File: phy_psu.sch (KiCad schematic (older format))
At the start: 54 parts

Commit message: sch: Make ERC happy with dummy power outputs
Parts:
- added DS? (x4): DummySupply, symbol pimouss-motherboard:DummySupply
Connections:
- net +1V8A: now also DS?.~ (Dummy)
- net +3V3A: now also DS?.~ (Dummy)
- net VphyDVDD: now also DS?.~ (Dummy)
- net VphyVDDC: now also DS?.~ (Dummy)
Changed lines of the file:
@@
 	8600 2900 8600 2950
 Connection ~ 8600 2900
+$Comp
+L pimouss-motherboard:DummySupply DS?
+U 1 1 5E44288B
+P 2400 1600
+F 0 "DS?" H 2400 1600 50  0001 C CNN
+F 1 "DummySupply" H 2400 1600 50  0001 C CNN
+F 2 "" H 2400 1600 50  0001 C CNN
+F 3 "" H 2400 1600 50  0001 C CNN
+	1    2400 1600
+	0    1    1    0
+$EndComp
+$Comp
+L pimouss-motherboard:DummySupply DS?
+U 1 1 5E443971
+P 2400 2800
+F 0 "DS?" H 2400 2800 50  0001 C CNN
+F 1 "DummySupply" H 2400 2800 50  0001 C CNN
+F 2 "" H 2400 2800 50  0001 C CNN
+F 3 "" H 2400 2800 50  0001 C CNN
+	1    2400 2800
+	0    1    1    0
+$EndComp
+$Comp
+L pimouss-motherboard:DummySupply DS?
+U 1 1 5E444394
+P 2400 4000
+F 0 "DS?" H 2400 4000 50  0001 C CNN
+F 1 "DummySupply" H 2400 4000 50  0001 C CNN
+F 2 "" H 2400 4000 50  0001 C CNN
+F 3 "" H 2400 4000 50  0001 C CNN
+	1    2400 4000
+	0    1    1    0
+$EndComp
+$Comp
+L pimouss-motherboard:DummySupply DS?
+U 1 1 5E444BDF
+P 2400 5200
+F 0 "DS?" H 2400 5200 50  0001 C CNN
+F 1 "DummySupply" H 2400 5200 50  0001 C CNN
+F 2 "" H 2400 5200 50  0001 C CNN
+F 3 "" H 2400 5200 50  0001 C CNN
+	1    2400 5200
+	0    1    1    0
+$EndComp
 $EndSCHEMATC

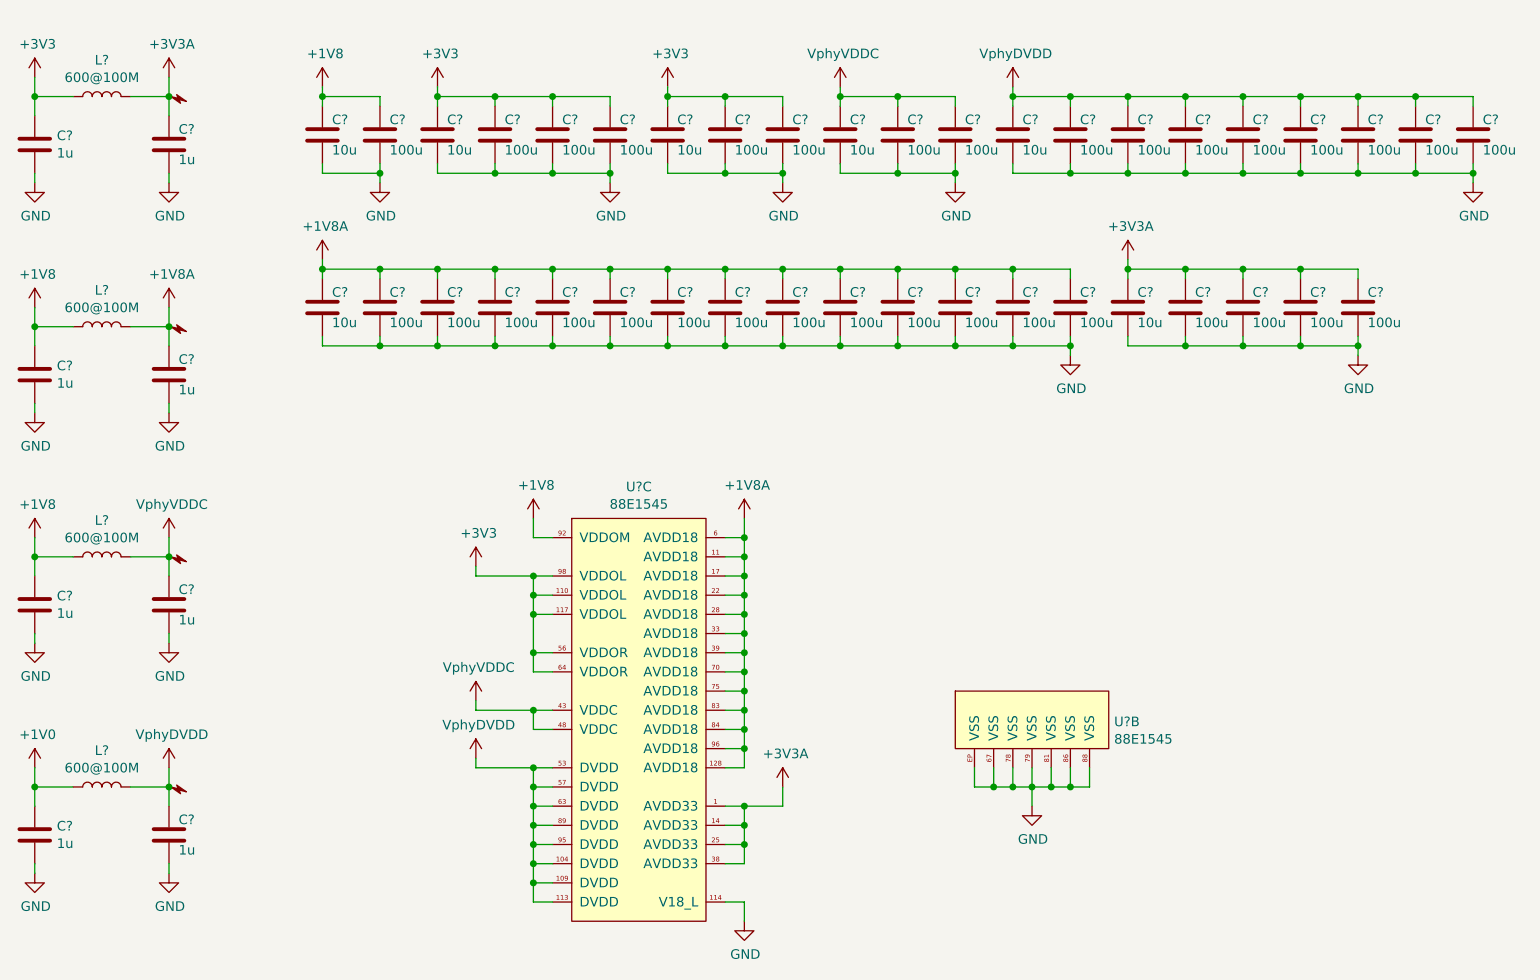
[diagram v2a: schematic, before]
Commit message: sch: Annotate & associate symbols with footprints
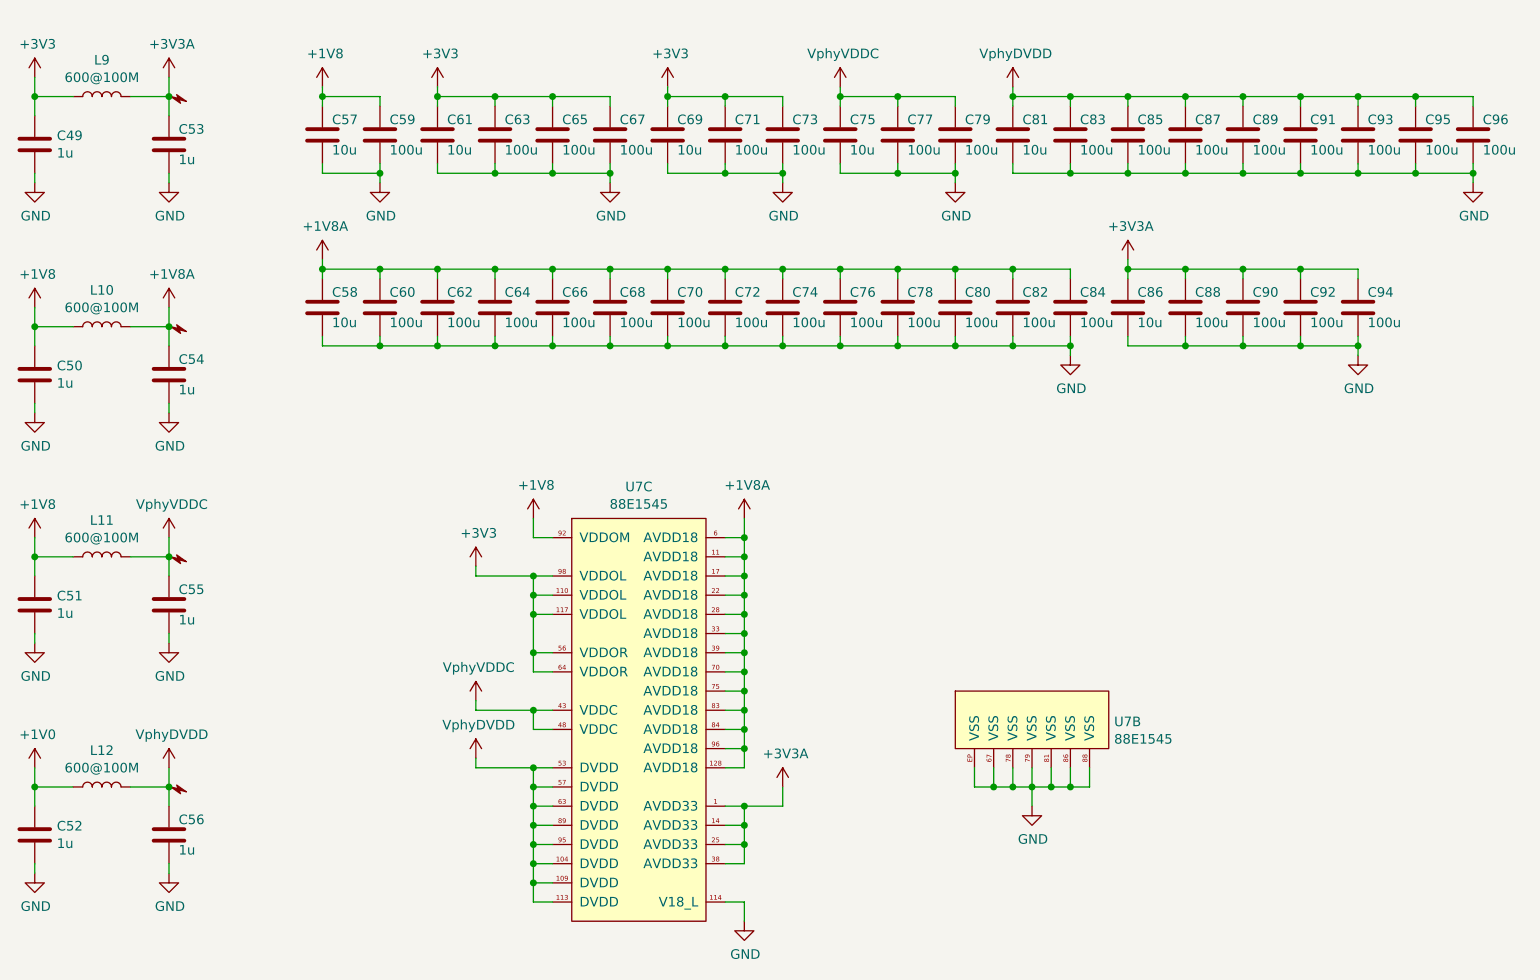
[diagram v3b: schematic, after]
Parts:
- removed DS? (x4): DummySupply, symbol pimouss-motherboard:DummySupply
- C49, C50, C51, C52, C53, C54, C55, C56, C57, C58, C59, C60, C61, C62, C63, C64, C65, C66, C67, C68, C69, C70, C71, C72, C73, C74, C75, C76, C77, C78, C79, C80, C81, C82, C83, C84, C85, C86, C87, C88, C89, C90, C91, C92, C93, C94, C95, C96: renamed from C?; footprint (none) -> Capacitor_SMD:C_0603_1608Metric
- L10, L11, L12, L9: renamed from L?; footprint (none) -> Inductor_SMD:L_0603_1608Metric
- gave numbers to parts that had none: 1

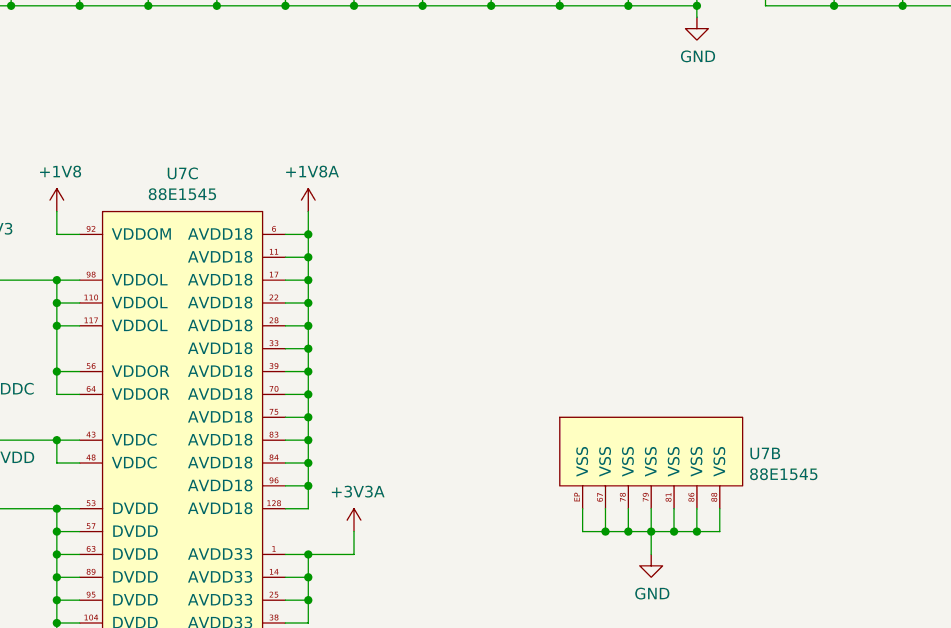
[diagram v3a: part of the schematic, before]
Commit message: lib, sch: Fix connectors refdes letter
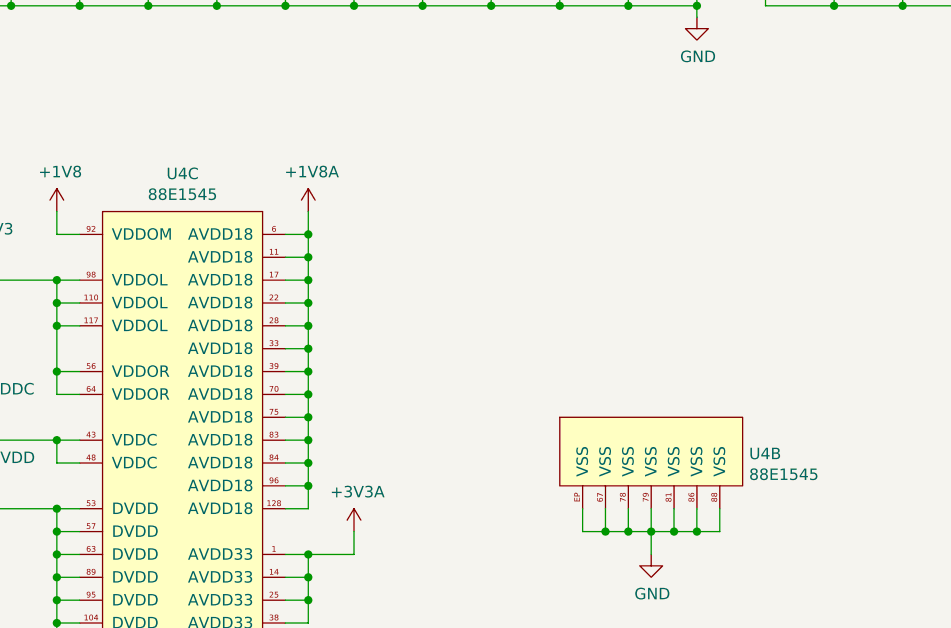
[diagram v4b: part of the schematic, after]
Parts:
- renumbered U7 to U4
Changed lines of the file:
@@
 $EndDescr
 $Comp
-L pimouss-motherboard:88E1545 U7
+L pimouss-motherboard:88E1545 U4
 U 2 1 5C7D4C8A
 P 6500 4700
-F 0 "U7" H 7328 4540 50  0000 L CNN
+F 0 "U4" H 7328 4540 50  0000 L CNN
 F 1 "88E1545" H 7328 4449 50  0000 L CNN
 F 2 "pimouss-motherboard:LQFP-128-1EP_14x20mm_P0.5mm_EP3.93x6.42mm" H 7950 2900 50  0001 C CNN
@@
 $EndComp
 $Comp
-L pimouss-motherboard:88E1545 U7
+L pimouss-motherboard:88E1545 U4
 U 3 1 5C7D4CD7
 P 4500 3800
-F 0 "U7" H 4850 3965 50  0000 C CNN
+F 0 "U4" H 4850 3965 50  0000 C CNN
 F 1 "88E1545" H 4850 3874 50  0000 C CNN
 F 2 "pimouss-motherboard:LQFP-128-1EP_14x20mm_P0.5mm_EP3.93x6.42mm" H 5950 2000 50  0001 C CNN

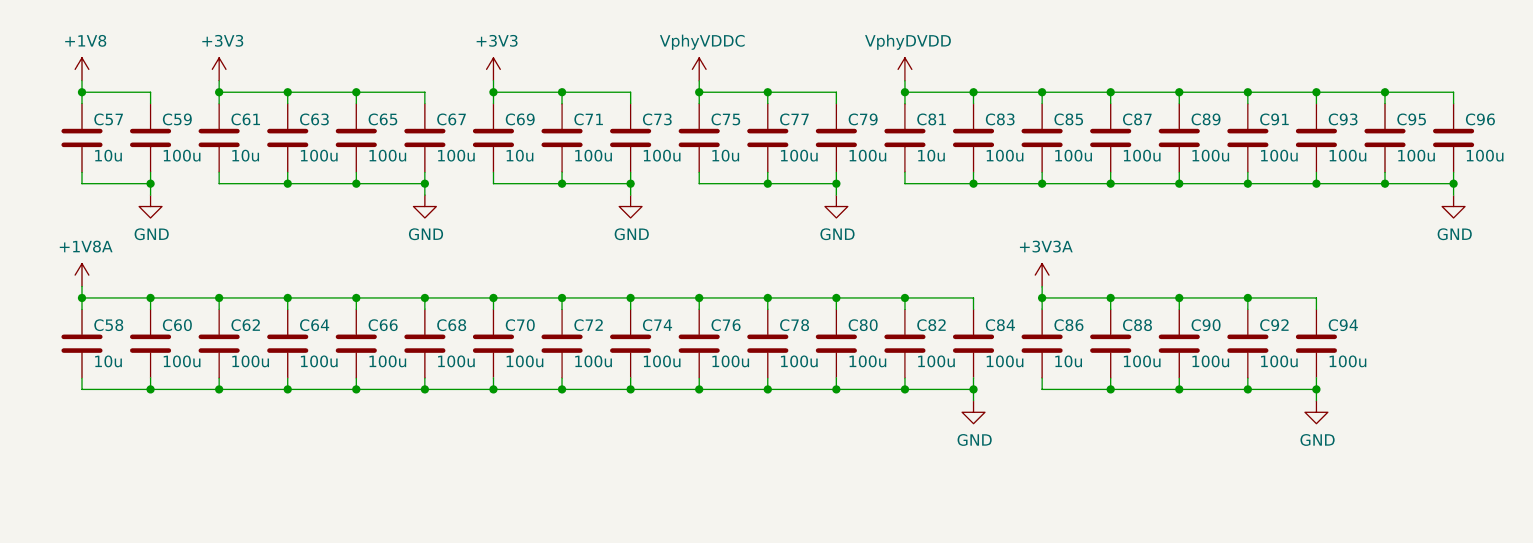
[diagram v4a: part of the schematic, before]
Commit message: sch: Change PHY decoupling caps from 100u to 100n
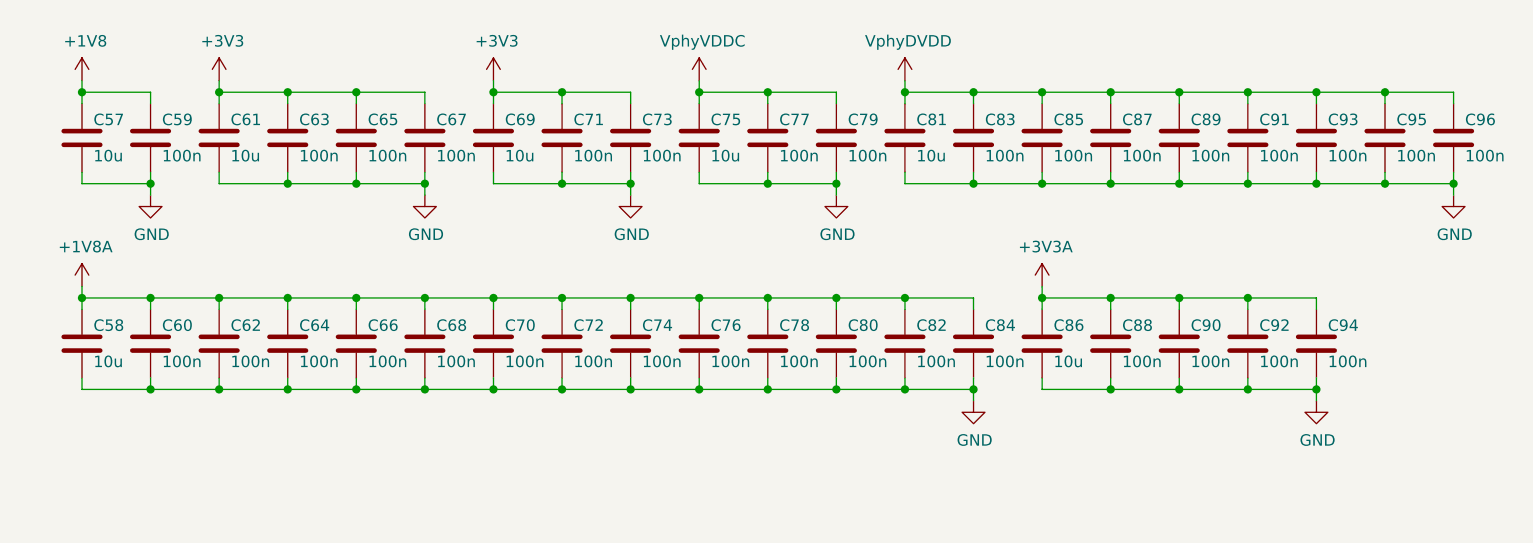
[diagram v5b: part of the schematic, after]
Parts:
- C59, C60, C62, C63, C64, C65, C66, C67, C68, C70, C71, C72, C73, C74, C76, C77, C78, C79, C80, C82, C83, C84, C85, C87, C88, C89, C90, C91, C92, C93, C94, C95, C96: value 100u -> 100n
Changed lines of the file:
@@
 P 3500 1800
 F 0 "C59" H 3550 1850 50  0000 L BNN
-F 1 "100u" H 3550 1750 50  0000 L TNN
+F 1 "100n" H 3550 1750 50  0000 L TNN
 F 2 "Capacitor_SMD:C_0603_1608Metric" H 3538 1650 50  0001 C CNN
 F 3 "~" H 3500 1800 50  0001 C CNN
@@
 P 4100 1800
 F 0 "C63" H 4150 1850 50  0000 L BNN
-F 1 "100u" H 4150 1750 50  0000 L TNN
+F 1 "100n" H 4150 1750 50  0000 L TNN
 F 2 "Capacitor_SMD:C_0603_1608Metric" H 4138 1650 50  0001 C CNN
 F 3 "~" H 4100 1800 50  0001 C CNN
@@
 P 4400 1800
 F 0 "C65" H 4450 1850 50  0000 L BNN
-F 1 "100u" H 4450 1750 50  0000 L TNN
+F 1 "100n" H 4450 1750 50  0000 L TNN
 F 2 "Capacitor_SMD:C_0603_1608Metric" H 4438 1650 50  0001 C CNN
 F 3 "~" H 4400 1800 50  0001 C CNN
@@
 P 4700 1800
 F 0 "C67" H 4750 1850 50  0000 L BNN
-F 1 "100u" H 4750 1750 50  0000 L TNN
+F 1 "100n" H 4750 1750 50  0000 L TNN
 F 2 "Capacitor_SMD:C_0603_1608Metric" H 4738 1650 50  0001 C CNN
 F 3 "~" H 4700 1800 50  0001 C CNN
@@
 P 5300 1800
 F 0 "C71" H 5350 1850 50  0000 L BNN
-F 1 "100u" H 5350 1750 50  0000 L TNN
+F 1 "100n" H 5350 1750 50  0000 L TNN
 F 2 "Capacitor_SMD:C_0603_1608Metric" H 5338 1650 50  0001 C CNN
 F 3 "~" H 5300 1800 50  0001 C CNN
@@
 P 5600 1800
 F 0 "C73" H 5650 1850 50  0000 L BNN
-F 1 "100u" H 5650 1750 50  0000 L TNN
+F 1 "100n" H 5650 1750 50  0000 L TNN
 F 2 "Capacitor_SMD:C_0603_1608Metric" H 5638 1650 50  0001 C CNN
 F 3 "~" H 5600 1800 50  0001 C CNN
@@
 P 6200 1800
 F 0 "C77" H 6250 1850 50  0000 L BNN
-F 1 "100u" H 6250 1750 50  0000 L TNN
+F 1 "100n" H 6250 1750 50  0000 L TNN
 F 2 "Capacitor_SMD:C_0603_1608Metric" H 6238 1650 50  0001 C CNN
 F 3 "~" H 6200 1800 50  0001 C CNN
@@
 P 6500 1800
 F 0 "C79" H 6550 1850 50  0000 L BNN
-F 1 "100u" H 6550 1750 50  0000 L TNN
+F 1 "100n" H 6550 1750 50  0000 L TNN
 F 2 "Capacitor_SMD:C_0603_1608Metric" H 6538 1650 50  0001 C CNN
 F 3 "~" H 6500 1800 50  0001 C CNN
@@
 P 7100 1800
 F 0 "C83" H 7150 1850 50  0000 L BNN
-F 1 "100u" H 7150 1750 50  0000 L TNN
+F 1 "100n" H 7150 1750 50  0000 L TNN
 F 2 "Capacitor_SMD:C_0603_1608Metric" H 7138 1650 50  0001 C CNN
 F 3 "~" H 7100 1800 50  0001 C CNN
@@
 P 7400 1800
 F 0 "C85" H 7450 1850 50  0000 L BNN
-F 1 "100u" H 7450 1750 50  0000 L TNN
+F 1 "100n" H 7450 1750 50  0000 L TNN
 F 2 "Capacitor_SMD:C_0603_1608Metric" H 7438 1650 50  0001 C CNN
 F 3 "~" H 7400 1800 50  0001 C CNN
@@
 P 7700 1800
 F 0 "C87" H 7750 1850 50  0000 L BNN
-F 1 "100u" H 7750 1750 50  0000 L TNN
+F 1 "100n" H 7750 1750 50  0000 L TNN
 F 2 "Capacitor_SMD:C_0603_1608Metric" H 7738 1650 50  0001 C CNN
 F 3 "~" H 7700 1800 50  0001 C CNN
@@
 P 8000 1800
 F 0 "C89" H 8050 1850 50  0000 L BNN
-F 1 "100u" H 8050 1750 50  0000 L TNN
+F 1 "100n" H 8050 1750 50  0000 L TNN
 F 2 "Capacitor_SMD:C_0603_1608Metric" H 8038 1650 50  0001 C CNN
 F 3 "~" H 8000 1800 50  0001 C CNN
@@
 P 8300 1800
 F 0 "C91" H 8350 1850 50  0000 L BNN
-F 1 "100u" H 8350 1750 50  0000 L TNN
+F 1 "100n" H 8350 1750 50  0000 L TNN
 F 2 "Capacitor_SMD:C_0603_1608Metric" H 8338 1650 50  0001 C CNN
 F 3 "~" H 8300 1800 50  0001 C CNN
@@
 P 8600 1800
 F 0 "C93" H 8650 1850 50  0000 L BNN
-F 1 "100u" H 8650 1750 50  0000 L TNN
+F 1 "100n" H 8650 1750 50  0000 L TNN
 F 2 "Capacitor_SMD:C_0603_1608Metric" H 8638 1650 50  0001 C CNN
 F 3 "~" H 8600 1800 50  0001 C CNN
@@
 P 8900 1800
 F 0 "C95" H 8950 1850 50  0000 L BNN
-F 1 "100u" H 8950 1750 50  0000 L TNN
+F 1 "100n" H 8950 1750 50  0000 L TNN
 F 2 "Capacitor_SMD:C_0603_1608Metric" H 8938 1650 50  0001 C CNN
 F 3 "~" H 8900 1800 50  0001 C CNN
@@
 P 9200 1800
 F 0 "C96" H 9250 1850 50  0000 L BNN
-F 1 "100u" H 9250 1750 50  0000 L TNN
+F 1 "100n" H 9250 1750 50  0000 L TNN
 F 2 "Capacitor_SMD:C_0603_1608Metric" H 9238 1650 50  0001 C CNN
 F 3 "~" H 9200 1800 50  0001 C CNN
@@
 P 3500 2700
 F 0 "C60" H 3550 2750 50  0000 L BNN
-F 1 "100u" H 3550 2650 50  0000 L TNN
+F 1 "100n" H 3550 2650 50  0000 L TNN
 F 2 "Capacitor_SMD:C_0603_1608Metric" H 3538 2550 50  0001 C CNN
 F 3 "~" H 3500 2700 50  0001 C CNN
@@
 P 3800 2700
 F 0 "C62" H 3850 2750 50  0000 L BNN
-F 1 "100u" H 3850 2650 50  0000 L TNN
+F 1 "100n" H 3850 2650 50  0000 L TNN
 F 2 "Capacitor_SMD:C_0603_1608Metric" H 3838 2550 50  0001 C CNN
 F 3 "~" H 3800 2700 50  0001 C CNN
@@
 P 4100 2700
 F 0 "C64" H 4150 2750 50  0000 L BNN
-F 1 "100u" H 4150 2650 50  0000 L TNN
+F 1 "100n" H 4150 2650 50  0000 L TNN
 F 2 "Capacitor_SMD:C_0603_1608Metric" H 4138 2550 50  0001 C CNN
 F 3 "~" H 4100 2700 50  0001 C CNN
@@
 P 4400 2700
 F 0 "C66" H 4450 2750 50  0000 L BNN
-F 1 "100u" H 4450 2650 50  0000 L TNN
+F 1 "100n" H 4450 2650 50  0000 L TNN
 F 2 "Capacitor_SMD:C_0603_1608Metric" H 4438 2550 50  0001 C CNN
 F 3 "~" H 4400 2700 50  0001 C CNN
@@
 P 4700 2700
 F 0 "C68" H 4750 2750 50  0000 L BNN
-F 1 "100u" H 4750 2650 50  0000 L TNN
+F 1 "100n" H 4750 2650 50  0000 L TNN
 F 2 "Capacitor_SMD:C_0603_1608Metric" H 4738 2550 50  0001 C CNN
 F 3 "~" H 4700 2700 50  0001 C CNN
@@
 P 5000 2700
 F 0 "C70" H 5050 2750 50  0000 L BNN
-F 1 "100u" H 5050 2650 50  0000 L TNN
+F 1 "100n" H 5050 2650 50  0000 L TNN
 F 2 "Capacitor_SMD:C_0603_1608Metric" H 5038 2550 50  0001 C CNN
 F 3 "~" H 5000 2700 50  0001 C CNN
@@
 P 5300 2700
 F 0 "C72" H 5350 2750 50  0000 L BNN
-F 1 "100u" H 5350 2650 50  0000 L TNN
+F 1 "100n" H 5350 2650 50  0000 L TNN
 F 2 "Capacitor_SMD:C_0603_1608Metric" H 5338 2550 50  0001 C CNN
 F 3 "~" H 5300 2700 50  0001 C CNN
@@
 P 5600 2700
 F 0 "C74" H 5650 2750 50  0000 L BNN
-F 1 "100u" H 5650 2650 50  0000 L TNN
+F 1 "100n" H 5650 2650 50  0000 L TNN
 F 2 "Capacitor_SMD:C_0603_1608Metric" H 5638 2550 50  0001 C CNN
 F 3 "~" H 5600 2700 50  0001 C CNN
@@
 P 5900 2700
 F 0 "C76" H 5950 2750 50  0000 L BNN
-F 1 "100u" H 5950 2650 50  0000 L TNN
+F 1 "100n" H 5950 2650 50  0000 L TNN
 F 2 "Capacitor_SMD:C_0603_1608Metric" H 5938 2550 50  0001 C CNN
 F 3 "~" H 5900 2700 50  0001 C CNN
@@
 P 6200 2700
 F 0 "C78" H 6250 2750 50  0000 L BNN
-F 1 "100u" H 6250 2650 50  0000 L TNN
+F 1 "100n" H 6250 2650 50  0000 L TNN
 F 2 "Capacitor_SMD:C_0603_1608Metric" H 6238 2550 50  0001 C CNN
 F 3 "~" H 6200 2700 50  0001 C CNN
@@
 P 6500 2700
 F 0 "C80" H 6550 2750 50  0000 L BNN
-F 1 "100u" H 6550 2650 50  0000 L TNN
+F 1 "100n" H 6550 2650 50  0000 L TNN
 F 2 "Capacitor_SMD:C_0603_1608Metric" H 6538 2550 50  0001 C CNN
 F 3 "~" H 6500 2700 50  0001 C CNN
@@
 P 6800 2700
 F 0 "C82" H 6850 2750 50  0000 L BNN
-F 1 "100u" H 6850 2650 50  0000 L TNN
+F 1 "100n" H 6850 2650 50  0000 L TNN
 F 2 "Capacitor_SMD:C_0603_1608Metric" H 6838 2550 50  0001 C CNN
 F 3 "~" H 6800 2700 50  0001 C CNN
@@
 P 7100 2700
 F 0 "C84" H 7150 2750 50  0000 L BNN
-F 1 "100u" H 7150 2650 50  0000 L TNN
+F 1 "100n" H 7150 2650 50  0000 L TNN
 F 2 "Capacitor_SMD:C_0603_1608Metric" H 7138 2550 50  0001 C CNN
 F 3 "~" H 7100 2700 50  0001 C CNN
@@
 P 7700 2700
 F 0 "C88" H 7750 2750 50  0000 L BNN
-F 1 "100u" H 7750 2650 50  0000 L TNN
+F 1 "100n" H 7750 2650 50  0000 L TNN
 F 2 "Capacitor_SMD:C_0603_1608Metric" H 7738 2550 50  0001 C CNN
 F 3 "~" H 7700 2700 50  0001 C CNN
@@
 P 8000 2700
 F 0 "C90" H 8050 2750 50  0000 L BNN
-F 1 "100u" H 8050 2650 50  0000 L TNN
+F 1 "100n" H 8050 2650 50  0000 L TNN
 F 2 "Capacitor_SMD:C_0603_1608Metric" H 8038 2550 50  0001 C CNN
 F 3 "~" H 8000 2700 50  0001 C CNN
@@
 P 8300 2700
 F 0 "C92" H 8350 2750 50  0000 L BNN
-F 1 "100u" H 8350 2650 50  0000 L TNN
+F 1 "100n" H 8350 2650 50  0000 L TNN
 F 2 "Capacitor_SMD:C_0603_1608Metric" H 8338 2550 50  0001 C CNN
 F 3 "~" H 8300 2700 50  0001 C CNN
@@
 P 8600 2700
 F 0 "C94" H 8650 2750 50  0000 L BNN
-F 1 "100u" H 8650 2650 50  0000 L TNN
+F 1 "100n" H 8650 2650 50  0000 L TNN
 F 2 "Capacitor_SMD:C_0603_1608Metric" H 8638 2550 50  0001 C CNN
 F 3 "~" H 8600 2700 50  0001 C CNN
